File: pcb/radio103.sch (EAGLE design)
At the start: 11 parts, among them IC1 LM833D, IC2 LM833D, IC3 74ACT00D, IC4 MCP23S17SO, IC5 LM386M-1, U1 FST3253

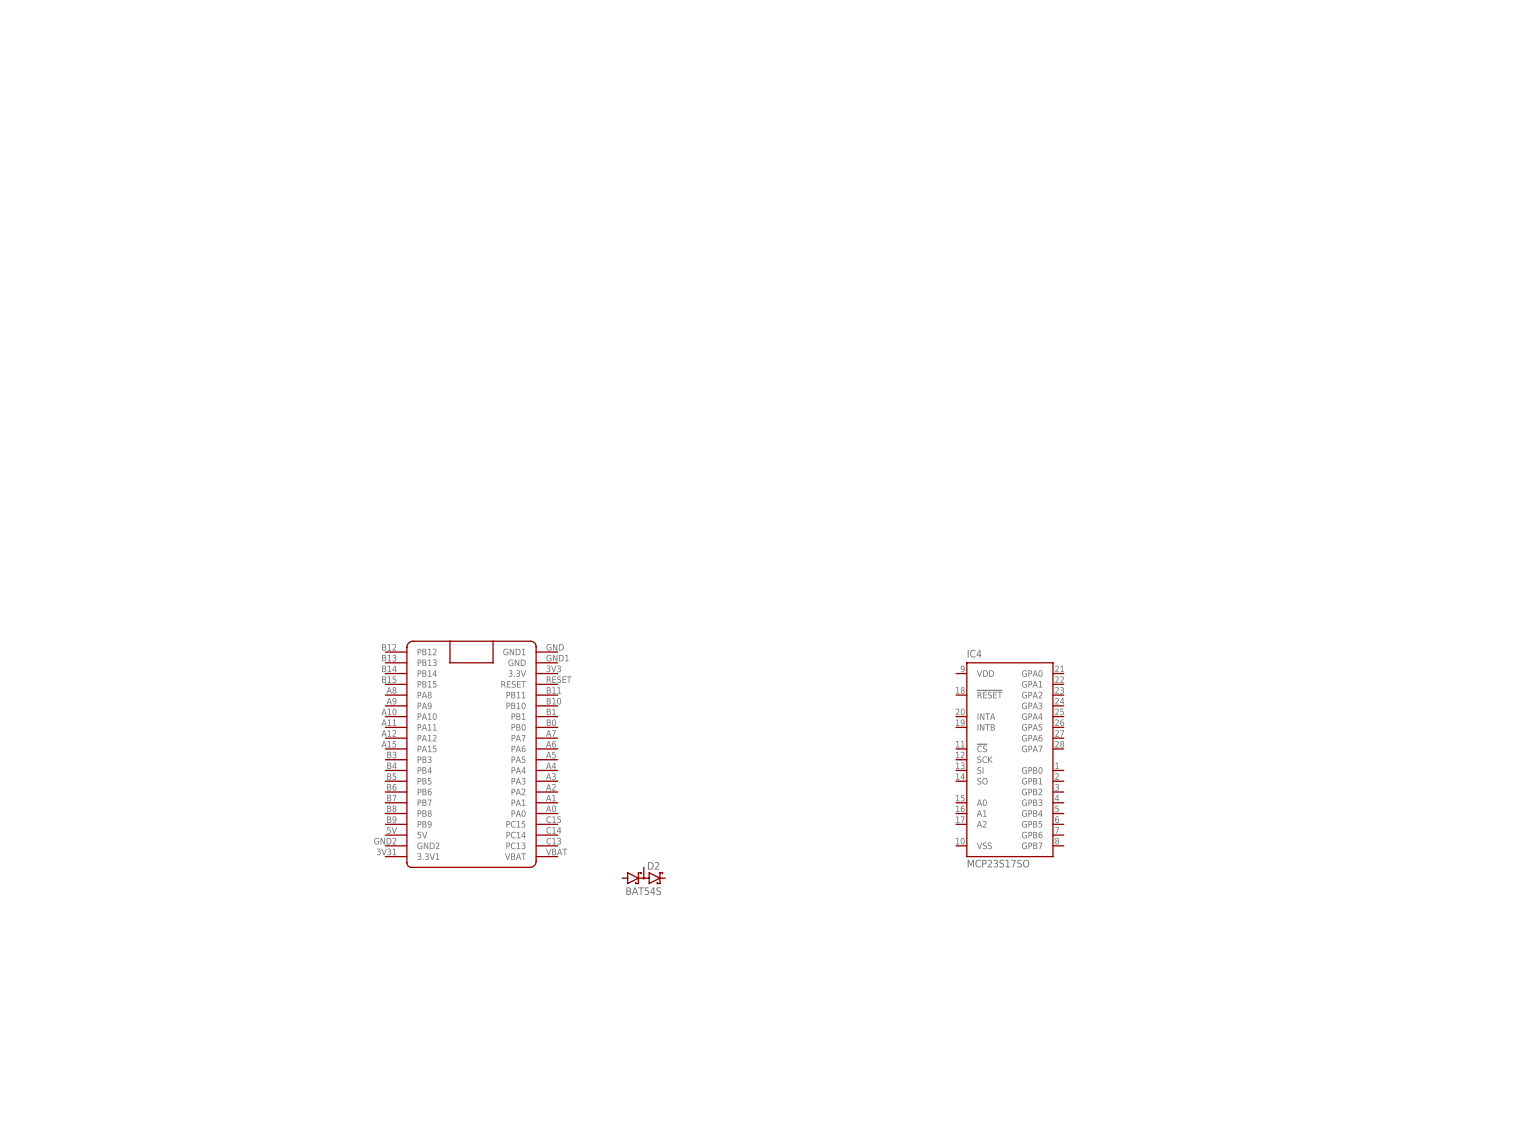
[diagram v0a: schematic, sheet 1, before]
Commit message: MCP23S17 + CD4066 + decimation works!
don't use remapped SPI1 w/ I2C1!
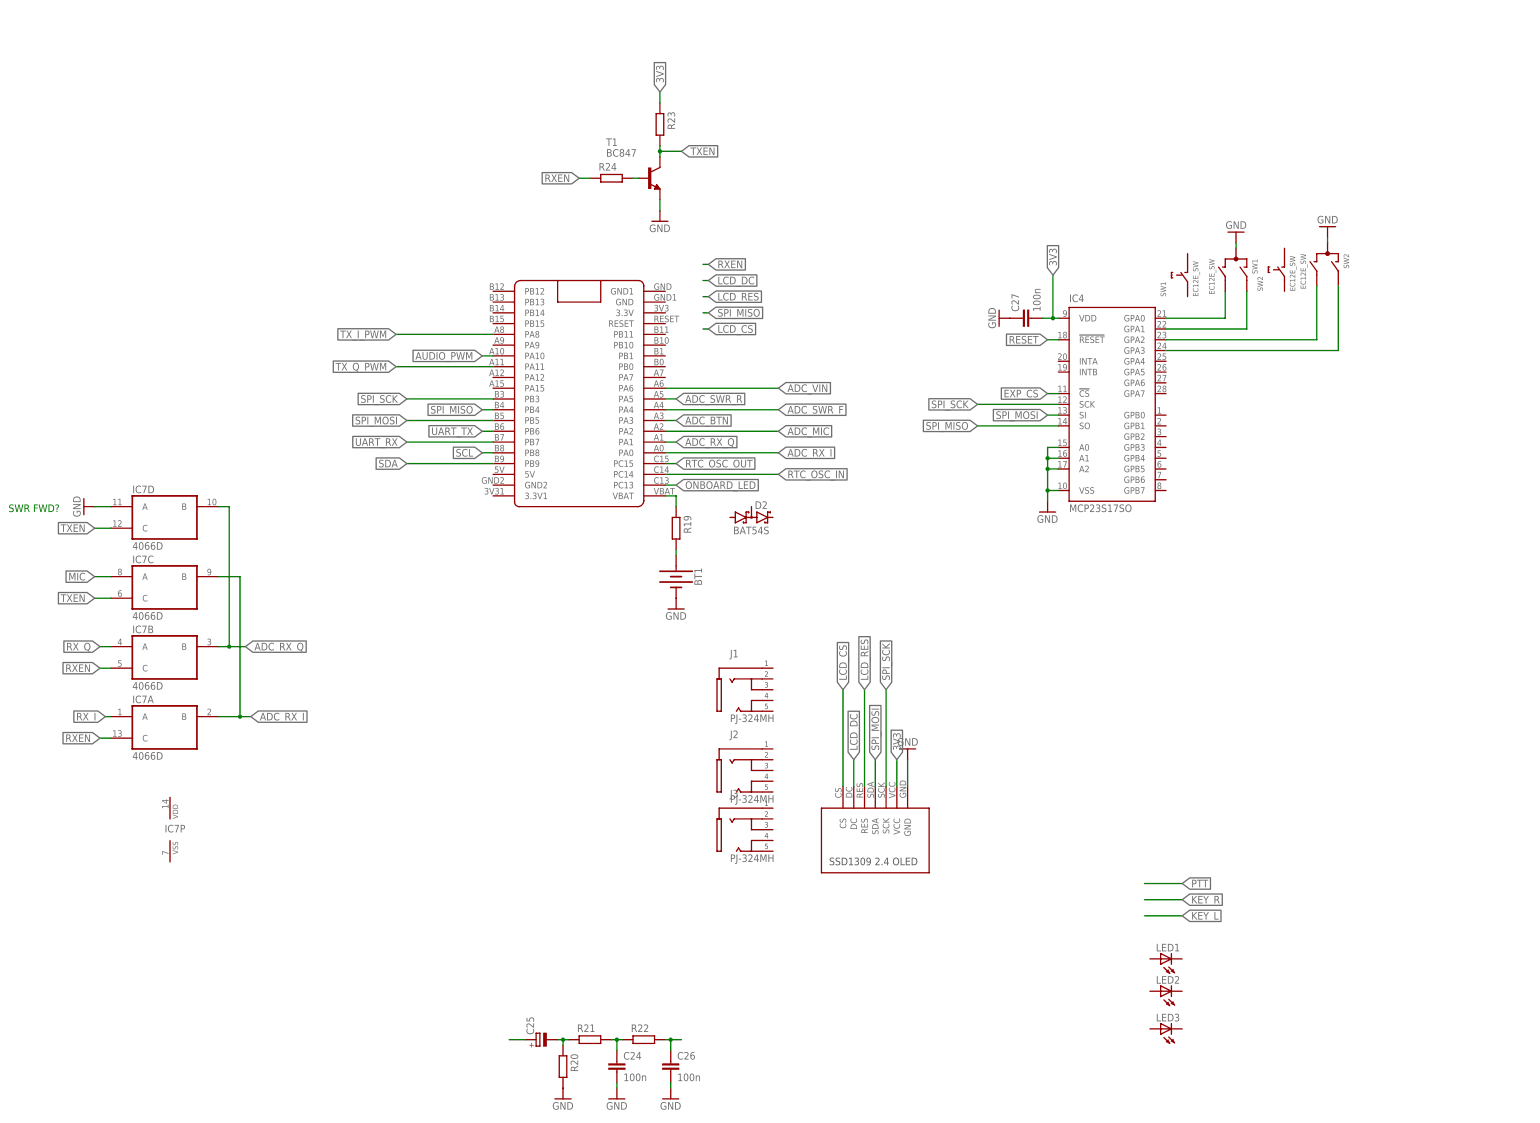
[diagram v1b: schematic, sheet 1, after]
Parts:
- added BT1: (no value), SparkFun-Batteries:BATTERY-12MM_SMD
- added C1, C10, C11, C12, C13, C14, C15, C18, C19, C2, C20, C21, C22, C23, C24, C26, C27, C3, C4, C5, C6, C7, C8, C9: 100n, rcl:C-EUC0805K
- added C16, C17, C25: (no value), rcl:CPOL-EUE2,5-6E
- added D3: BAT54S, diode:BAT54S
- added H1, H2: MOUNT-HOLE3.0, holes:MOUNT-HOLE3.0
- added IC6: LM1117MPX-3.3, lm1117:LM1117MPX-3.3
- added IC7: 4066D, 40xx:4066D
- added J1, J2, J3: PJ-324MH, ub0baa:PJ-324MH
- added JP1, JP2: (no value), pinhead:PINHD-1X1
- added JP3: (no value), pinhead:PINHD-1X2
- added LED1, LED2, LED3: (no value), led-smd:OSYG1608
- added R1, R10, R11, R12, R13, R14, R15, R16, R17, R18, R19, R2, R20, R21, R22, R23, R24, R3, R4, R5, R6, R7, R8, R9: (no value), rcl:R-EU_R0805
- added SJ1, SJ2, SJ3, SJ4: (no value), jumper:SJ
- added SW1, SW2: EC12E_SW, switch-alps:EC12E_SW
- added T1: BC847, transistor:BC847
- added U$4: SSD1309_2.4_OLED, ub0baa:SSD1309_2.4_OLED
- IC2: value LM833D -> 7805TV; device linear:LM833D -> linear:7805TV
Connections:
- new net 3V3: C1.2, C13.2, C2.2, C22.2, C27.2, D1.C2, D3.C2, IC3P.VCC, IC4.VDD, IC6.OUT, IC6.OUT1, R12.2, R23.2, R7.2, R9.2, U$2.GND, U$4.VCC, U1.VCC
- new net 5V: C19.1, C23.2, IC2.VO, IC5.VS, IC6.IN, U$3.OUT-.1, U$3.OUT-.2
- new net ADC_BTN: U$1.PA3
- new net ADC_I1: C8.1, D1.C1A2, R14.1, R7.1, R8.2
- new net ADC_MIC: U$1.PA2
- new net ADC_Q1: C9.1, D3.C1A2, R10.2, R15.1, R9.1
- new net ADC_RX_I: IC7A.B, IC7C.B, U$1.PA0
- new net ADC_RX_Q: IC7B.B, IC7D.B, U$1.PA1
- new net ADC_SWR_F: U$1.PA4
- new net ADC_SWR_R: U$1.PA5
- new net ADC_VIN: U$1.PA6
- new net AUDIO: IC5.+IN
- new net AUDIO_PWM: U$1.PA10
- new net EXP_CS: IC4.!CS
- new net GND: BT1.-, C1.1, C12.1, C13.1, C14.1, C18.2, C19.2, C2.1, C21.1, C22.1, C23.1, C24.2, C26.2, C27.1, C3.2, C4.2, C5.1, C6.1, D1.A1, D3.A1, IC1P.V-, IC2.GND, IC3P.GND, IC4.A0, IC4.A1, IC4.A2, IC4.VSS, IC5.-IN, IC5.GND, IC6.GND, IC7D.A, JP3.2, R10.1, R13.2, R16.1, R20.1, R8.1, SW1G$1.C, SW2G$1.C, T1.E, U$2.VIN, U$3.IN+.1, U$3.IN+.2, U$3.OUT+.1, U$3.OUT+.2, U$4.GND, U1.GND, U1.~OE1, U1.~OE2
- new net LCD_CS: U$4.CS
- new net LCD_DC: U$4.DC
- new net LCD_RES: U$4.RES
- new net MIC: IC7C.A
- new net N$1: C3.1, R1.1, U1.2B1
- new net N$10: C7.1, C8.2, IC1B.OUT, R5.2
- new net N$12: C11.2, R11.2, U1.2A
- new net N$13: U$2.1, U1.S1
- new net N$14: C12.2, R11.1, R12.1, R13.1
- new net N$15: U$2.0, U1.S0
- new net N$16: IC4.GPA0, SW1G$1.B
- new net N$17: IC3C.O, U1.1B1
- new net N$18: IC3D.O, U1.1B2
- new net N$19: C17.+, IC5.GAIN@1
- new net N$2: C4.1, R2.1, U1.2B2
- new net N$20: IC5.GAIN@2, R17.1, SJ2.1
- new net N$21: C17.-, R17.2, SJ2.2
- new net N$22: C18.1, IC5.BYPASS
- new net N$23: C16.+, IC5.OUT
- new net N$24: C15.1, C16.-, JP3.1
- new net N$25: C15.2, R16.2
- new net N$26: IC3A.I1, SJ1.2, U$2.2
- new net N$27: IC3A.I0, SJ1.1, SJ4.2
- new net N$28: IC3A.O, IC3B.I1, SJ3.2
- new net N$29: IC3B.I0, SJ3.1
- new net N$3: C5.2, R3.1, U1.2B3
- new net N$30: C20.2, IC3B.O, R18.1
- new net N$31: SJ4.1, U1.1A
- new net N$32: C25.-, R20.2, R21.2
- new net N$33: C24.1, R21.1, R22.2
- new net N$34: C26.1, R22.1
- new net N$35: C25.+
- new net N$36: BT1.+, R19.1
- new net N$37: R19.2, U$1.VBAT
- new net N$38: IC4.GPA1, SW1G$1.A
- new net N$39: R24.1, T1.B
- new net N$4: C6.2, R4.1, U1.2B4
- new net N$40: IC4.GPA2, SW2G$1.B
- new net N$41: IC4.GPA3, SW2G$1.A
- new net N$5: C10.2, IC1A.-IN, R1.2, R6.1
- new net N$6: IC1B.+IN, R2.2
- new net N$7: C7.2, IC1B.-IN, R3.2, R5.1
- new net N$8: IC1A.+IN, R4.2
- new net N$9: C10.1, C9.2, IC1A.OUT, R6.2
- new net ONBOARD_LED: U$1.PC13
- new net RESET: IC4.!RESET
- new net RTC_OSC_IN: U$1.PC14
- new net RTC_OSC_OUT: U$1.PC15
- new net RX: C11.1
- new net RXEN: IC7A.C, IC7B.C, R24.2
- new net RX_I: IC7A.A, R14.2
- new net RX_Q: IC7B.A, R15.2
- new net SCL: U$1.PB8, U$2.SCL
- new net SDA: U$1.PB9, U$2.SDA
- new net SPI_MISO: IC4.SO, U$1.PB4
- new net SPI_MOSI: IC4.SI, U$1.PB5, U$4.SDA
- new net SPI_SCK: IC4.SCK, U$1.PB3, U$4.SCK
- new net TX: C20.1, R18.2
- new net TXEN: IC7C.C, IC7D.C, R23.1, T1.C
- new net TX_I: IC3D.I0, IC3D.I1, U1.1B4
- new net TX_I_PWM: U$1.PA8
- new net TX_Q: IC3C.I0, IC3C.I1, U1.1B3
- new net TX_Q_PWM: U$1.PA11
- new net UART_RX: U$1.PB7
- new net UART_TX: U$1.PB6
- new net VIN: C21.2, IC2.VI, U$3.IN-.1, U$3.IN-.2
- new net VOPAMP: C14.2, IC1P.V+
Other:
- note added: "SWR FWD?"
- moved on the sheet: D1, D2, IC1A, IC1B, IC3A, IC3B, IC3C, IC3D, IC3P, IC4

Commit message: MCP encoder + mic amp
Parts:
- added C28, C31: 100n, rcl:C-EUC0805K
- added C29, C30, C32: (no value), rcl:CPOL-EUE2,5-6E
- added CON1: XT30PW-M, amass:XT30PW-M
- added D4: BAT54S, diode:BAT54S
- added IC8: LM833D, linear:LM833D
- added JP4: (no value), pinhead:PINHD-1X2
- added R25, R26, R27, R28, R29, R30, R31, R32, R33, R34, R35, R36, R37, R38, R39, R40: (no value), rcl:R-EU_R0805
- added S1, S2, S3, S4: (no value), switch-omron:10-XX
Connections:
- removed net ADC_MIC: U$1.PA2
- new net N$42: R26.1, R27.2, S2.S, S2.S1
- new net N$43: R31.1, R32.2, R33.1
- new net N$44: R27.1, R28.2, S3.S, S3.S1
- new net N$45: R28.1, R29.2, S4.S, S4.S1
- new net N$46: R29.1, R30.2, SW1G$2.1
- new net N$47: R30.1, SW2G$2.1
- new net N$48: C30.+, IC8A.+IN, R35.2, R36.1
- new net N$49: C31.1, IC8A.-IN, R34.2, R37.2
- new net N$50: C31.2, IC8A.OUT, R34.1, R39.2
- new net N$51: C29.-, R37.1
- new net N$52: C29.+, JP4.2, R38.2
- new net N$53: C32.-, R39.1
- new net N$54: C32.+, R40.1
- new net VBAT: R31.2
- net 3V3: now also D4.C2, R25.2, U$1.3.3V
- net ADC_BTN: now also R25.1, R26.2, S1.S, S1.S1
- net ADC_VIN: now also R33.2
- net GND: now also C28.1, C30.-, D4.A1, IC8P.V-, JP4.1, R32.1, R36.2, R40.2, S1.P, S1.P1, S2.P, S2.P1, S3.P, S3.P1, S4.P, S4.P1, SW1G$2.2, SW2G$2.2, U$1.GND, U$1.GND1
- net RESET: now also U$1.RESET
- net RXEN: now also R23.1, T1.C; no longer R24.2
- net TXEN: now also R24.2; no longer R23.1, T1.C
- net VOPAMP: now also C28.2, IC8P.V+, R35.1, R38.1
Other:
- moved on the sheet: SW1, SW2

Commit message: fonts + font generator + UI layout
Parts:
- added D5, D6, D7, D8: BAT54S, diode:BAT54S
- added IC10: 78L05Z, linear:78L05Z
- added IC9: 78L08Z, linear:78L08Z
- added R41, R42, R43, R44: (no value), rcl:R-EU_R0805
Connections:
- new net N$55: D5.C1A2, IC4.GPA4, R43.1
- new net N$56: R43.2
- new net N$57: D6.C1A2, IC4.GPA5, R41.1
- new net N$58: R41.2
- new net N$59: D7.C1A2, IC4.GPA6, R42.1
- new net N$60: R42.2
- new net N$61: D8.C1A2, IC4.GPA7, R44.1
- new net N$62: R44.2
- net 3V3: now also D5.C2, D6.C2, D7.C2, D8.C2
- net GND: now also D5.A1, D6.A1, D7.A1, D8.A1
- net N$43: now also D4.C1A2
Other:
- note added: "78M08 DPAK?"
- moved on the sheet: SW2

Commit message: gfx improved
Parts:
- added C33, C34, C35, C36, C37, C38: 100n, rcl:C-EUC0805K
- added IC11: LM833D, linear:LM833D
- added R45, R46, R47, R48, R49, R50: (no value), rcl:R-EU_R0805
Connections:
- new net N$63: C33.2, IC11A.+IN, R45.2
- new net N$64: C35.1, R45.1, R46.2
- new net N$65: C35.2, IC11A.-IN, IC11A.OUT, R50.1
- new net N$66: C38.1, R48.1, R49.2
- new net N$67: C34.2, R46.1, R47.2
- new net N$68: R47.1
- new net N$69: C37.2, R49.1, R50.2
- new net N$71: C36.2, IC11B.+IN, R48.2
- new net N$73: C38.2, IC11B.-IN, IC11B.OUT
- net GND: now also C33.1, C34.1, C36.1, C37.1

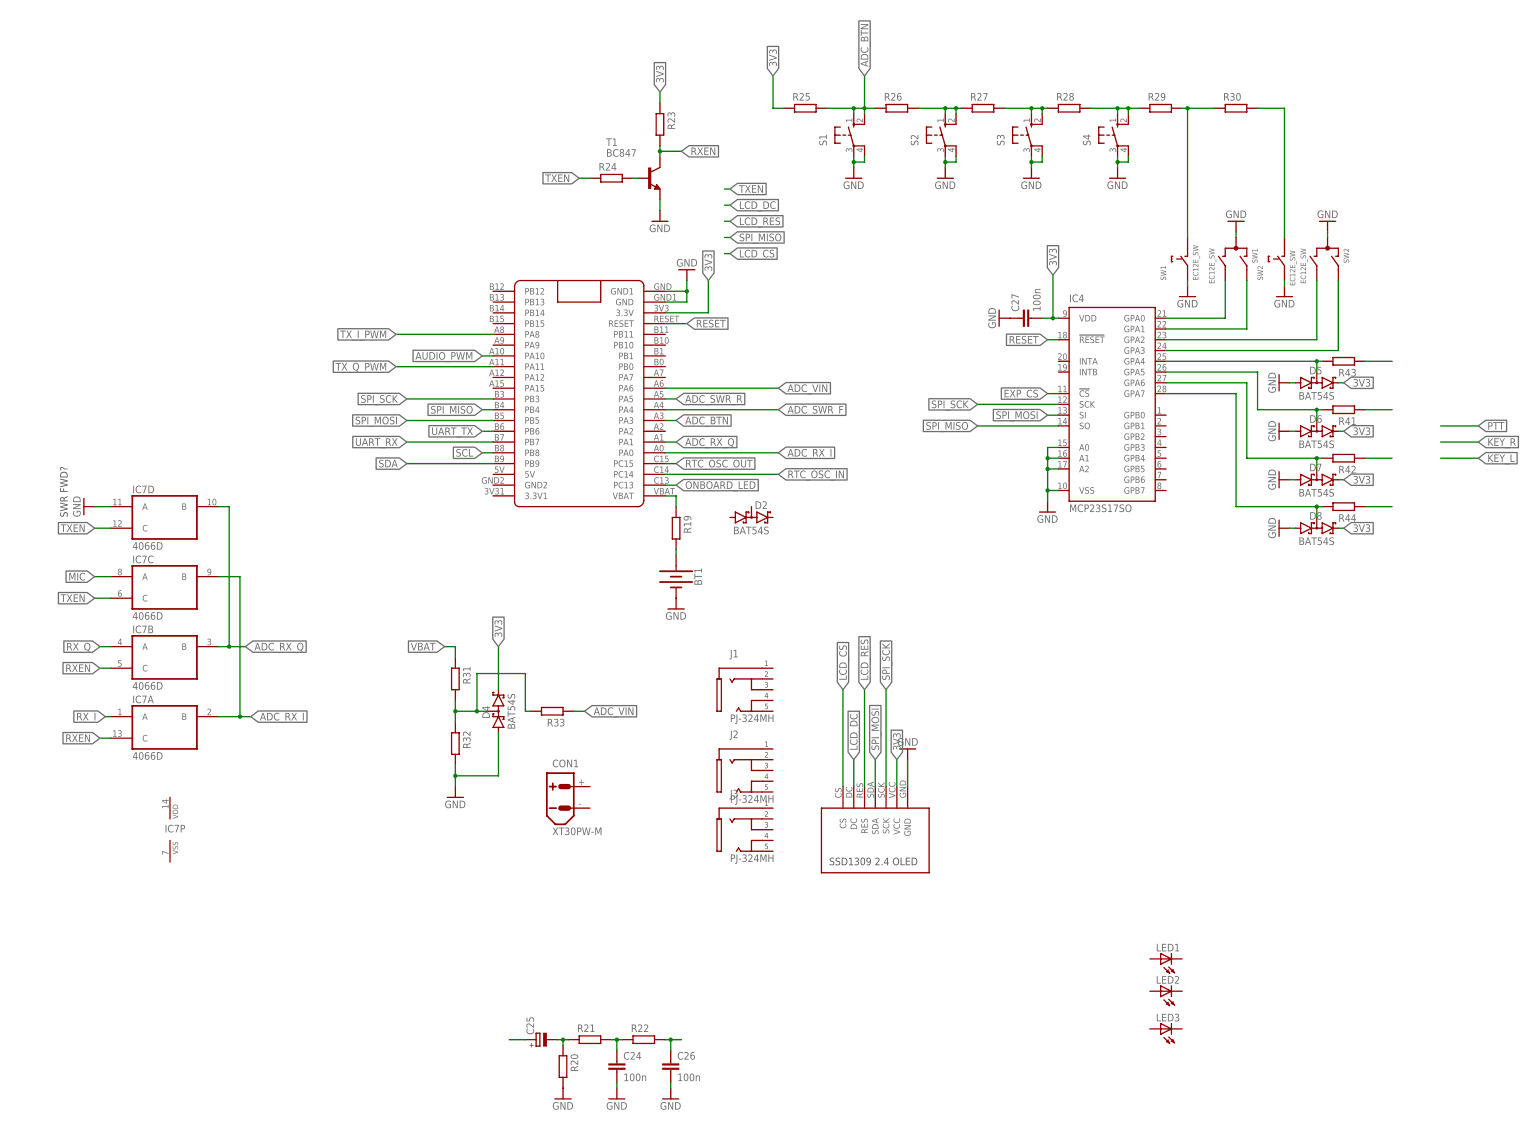
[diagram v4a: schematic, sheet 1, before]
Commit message: menu system + splash RLE
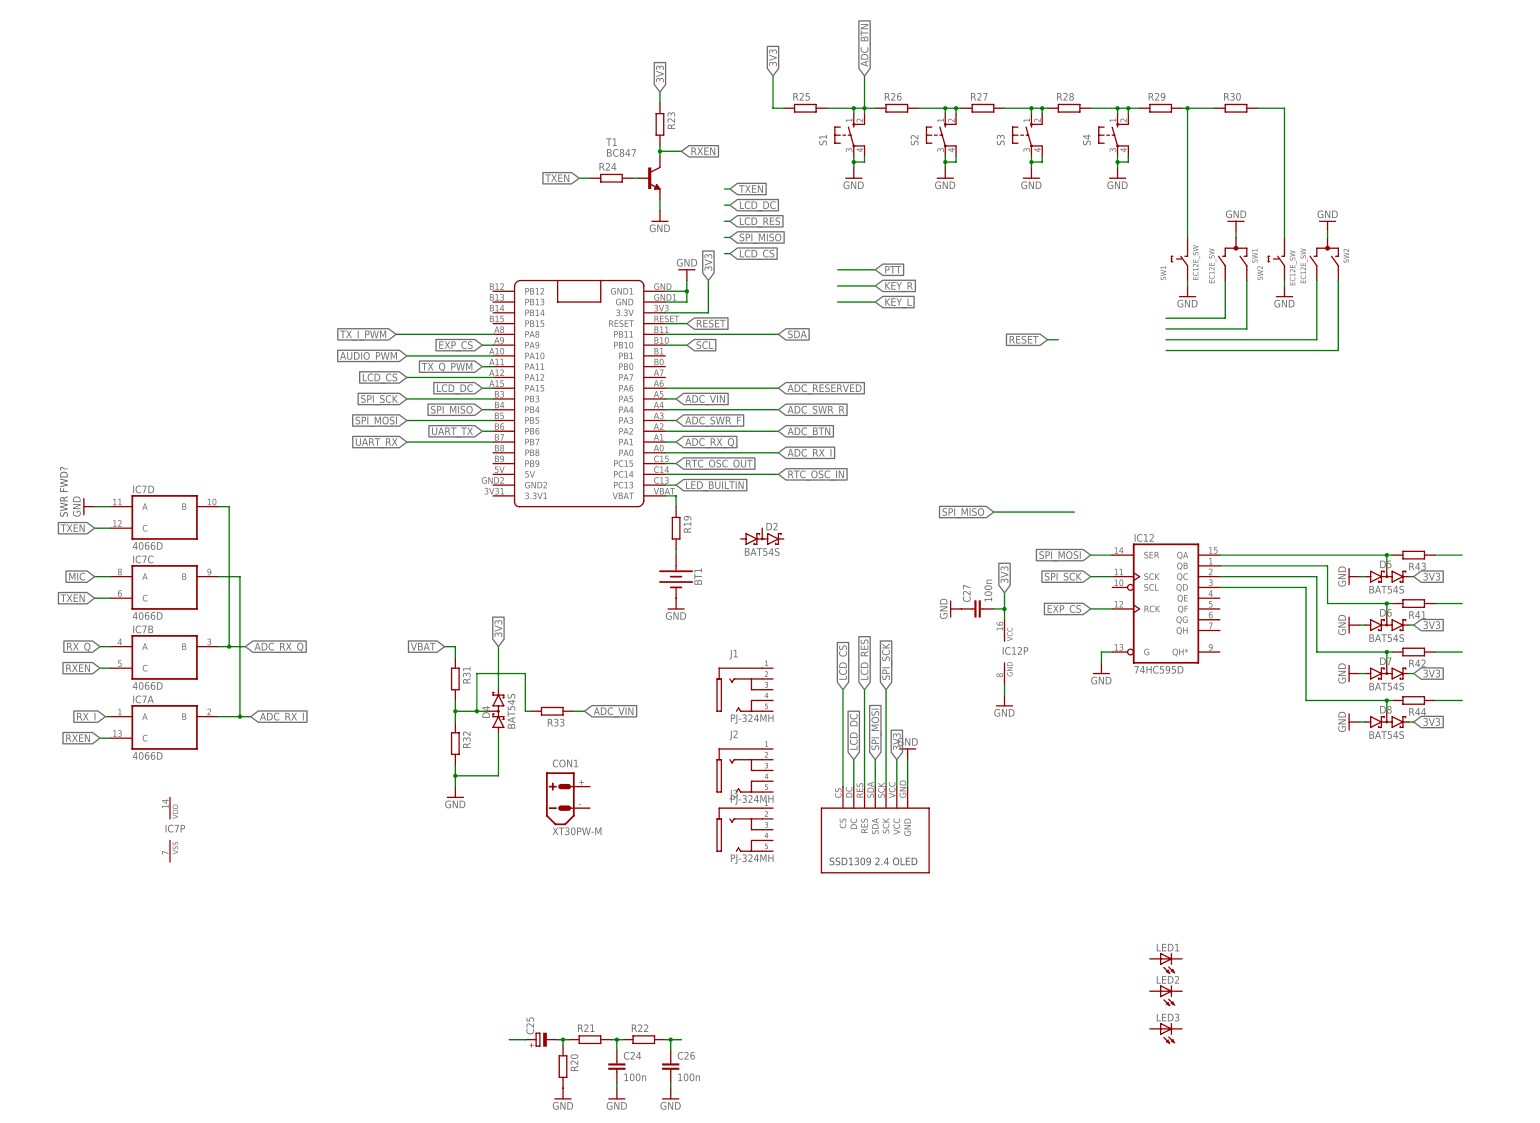
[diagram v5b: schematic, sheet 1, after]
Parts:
- removed IC4: MCP23S17SO, microchip:MCP23S17SO
- added IC12: 74HC595D, 74xx-eu:74HC595D
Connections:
- net ONBOARD_LED renamed LED_BUILTIN
- new net ADC_RESERVED: U$1.PA6
- net 3V3: now also IC12P.VCC; no longer IC4.VDD
- net ADC_BTN: now also U$1.PA2; no longer U$1.PA3
- net ADC_SWR_F: now also U$1.PA3; no longer U$1.PA4
- net ADC_SWR_R: now also U$1.PA4; no longer U$1.PA5
- net ADC_VIN: now also U$1.PA5; no longer U$1.PA6
- net EXP_CS: now also IC12A.RCK, U$1.PA9; no longer IC4.!CS
- net GND: now also IC12A.G, IC12P.GND; no longer IC4.A0, IC4.A1, IC4.A2, IC4.VSS
- net LCD_CS: now also U$1.PA12
- net LCD_DC: now also U$1.PA15
- net N$16: no longer IC4.GPA0
- net N$38: no longer IC4.GPA1
- net N$40: no longer IC4.GPA2
- net N$41: no longer IC4.GPA3
- net N$55: now also IC12A.QA; no longer IC4.GPA4
- net N$57: now also IC12A.QB; no longer IC4.GPA5
- net N$59: now also IC12A.QC; no longer IC4.GPA6
- net N$61: now also IC12A.QD; no longer IC4.GPA7
- net RESET: no longer IC4.!RESET
- net SCL: now also U$1.PB10; no longer U$1.PB8
- net SDA: now also U$1.PB11; no longer U$1.PB9
- net SPI_MISO: no longer IC4.SO
- net SPI_MOSI: now also IC12A.SER; no longer IC4.SI
- net SPI_SCK: now also IC12A.SCK; no longer IC4.SCK
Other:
- moved on the sheet: C27, D2, D5, D6, D7, D8, R41, R42, R43, R44

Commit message: test
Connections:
- net N$55: no longer IC12A.QA
- net N$57: no longer IC12A.QB
- net N$59: no longer IC12A.QC
- net N$61: no longer IC12A.QD
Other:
- moved on the sheet: D5, D6, D7, D8, J1, R41, R42, R43, R44
